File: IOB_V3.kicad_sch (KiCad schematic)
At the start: 6 parts, among them J1 Conn_01x02, J2 Conn_01x03, U1 REF3033

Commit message: WIP
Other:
- sheet MCU ports: added Vref_in; removed OCP_PWR_GOOD, SPI3_CLK, SPI3_MISO, SPI3_MOSI, SPI3_~{CS}

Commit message: WIP
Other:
- note added: "24V_PWR_Supply"

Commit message: WIP
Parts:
- added J18: Conn_01x08, Connector_IDC:IDC-Header_2x04_P2.54mm_Horizontal, symbol Connector_Generic:Conn_01x08
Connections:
- net GND: now also J18.8 (Pin_8)
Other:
- moved on the sheet: J2, U1

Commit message: WIP
for @Markus
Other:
- moved on the sheet: J1
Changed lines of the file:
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@@
     (comment 1 "Nathan Runggaldier")
   )
-  (junction (at 73.533 151.892) (diameter 0) (color 0 0 0 0)
+  (junction (at 71.247 151.892) (diameter 0) (color 0 0 0 0)
   )
   (junction (at 82.677 144.272) (diameter 0) (color 0 0 0 0)
@@
   )
   (junction (at 237.617 46.736) (diameter 0) (color 0 0 0 0)
-  )
-  (junction (at 71.501 144.272) (diameter 0) (color 0 0 0 0)
   )
   (junction (at 94.361 144.272) (diameter 0) (color 0 0 0 0)
@@
     (stroke (width 0) (type default) (color 0 0 0 0))
   )
-  (wire (pts (xy 71.501 144.272) (xy 71.501 144.399))
-    (stroke (width 0) (type default) (color 0 0 0 0))
-  )
   (wire (pts (xy 104.521 154.432) (xy 104.521 156.972))
     (stroke (width 0) (type default) (color 0 0 0 0))
@@
     (stroke (width 0) (type default) (color 0 0 0 0))
   )
-  (wire (pts (xy 73.533 151.892) (xy 73.533 153.289))
+  (wire (pts (xy 71.247 151.892) (xy 71.247 153.289))
     (stroke (width 0) (type default) (color 0 0 0 0))
   )
@@
     (stroke (width 0) (type default) (color 0 0 0 0))
   )
-  (wire (pts (xy 73.533 146.812) (xy 73.533 151.892))
+  (wire (pts (xy 71.247 146.812) (xy 71.247 151.892))
     (stroke (width 0) (type default) (color 0 0 0 0))
   )
@@
     (stroke (width 0) (type default) (color 0 0 0 0))
   )
+  (wire (pts (xy 69.215 144.272) (xy 82.677 144.272))
+    (stroke (width 0) (type default) (color 0 0 0 0))
+  )
   (wire (pts (xy 136.525 69.342) (xy 148.082 69.342))
     (stroke (width 0) (type default) (color 0 0 0 0))
   )
-  (wire (pts (xy 82.677 144.272) (xy 71.501 144.272))
-    (stroke (width 0) (type default) (color 0 0 0 0))
-  )
   (wire (pts (xy 198.12 97.663) (xy 188.595 97.663))
     (stroke (width 0) (type default) (color 0 0 0 0))
@@
     (stroke (width 0) (type default) (color 0 0 0 0))
   )
-  (wire (pts (xy 71.501 146.812) (xy 73.533 146.812))
+  (wire (pts (xy 69.215 146.812) (xy 71.247 146.812))
     (stroke (width 0) (type default) (color 0 0 0 0))
   )
@@
     (stroke (width 0) (type default) (color 0 0 0 0))
   )
-  (wire (pts (xy 73.533 151.892) (xy 66.421 151.892))
+  (wire (pts (xy 71.247 151.892) (xy 64.135 151.892))
     (stroke (width 0) (type default) (color 0 0 0 0))
   )
@@
     (effects (font (size 1.27 1.27)) (justify right bottom))
   )
-  (symbol (lib_id "power:GND") (at 73.533 153.289 0) (unit 1)
+  (symbol (lib_id "power:GND") (at 71.247 153.289 0) (unit 1)
     (in_bom yes) (on_board yes) (fields_autoplaced)
-    (property "Reference" "#PWR01" (id 0) (at 73.533 159.639 0)
-      (effects (font (size 1.27 1.27)) hide)
-    )
-    (property "Value" "GND" (id 1) (at 73.533 157.988 0))
-    (property "Footprint" "" (id 2) (at 73.533 153.289 0)
-      (effects (font (size 1.27 1.27)) hide)
-    )
-    (property "Datasheet" "" (id 3) (at 73.533 153.289 0)
+    (property "Reference" "#PWR01" (id 0) (at 71.247 159.639 0)
+      (effects (font (size 1.27 1.27)) hide)
+    )
+    (property "Value" "GND" (id 1) (at 71.247 157.988 0))
+    (property "Footprint" "" (id 2) (at 71.247 153.289 0)
+      (effects (font (size 1.27 1.27)) hide)
+    )
+    (property "Datasheet" "" (id 3) (at 71.247 153.289 0)
       (effects (font (size 1.27 1.27)) hide)
     )
@@
     (pin "3")
   )
-  (symbol (lib_id "Connector_Generic_MountingPin:Conn_01x02_MountingPin") (at 66.421 144.272 0) (mirror y) (unit 1)
+  (symbol (lib_id "Connector_Generic_MountingPin:Conn_01x02_MountingPin") (at 64.135 144.272 0) (mirror y) (unit 1)
     (in_bom yes) (on_board yes)
-    (property "Reference" "J1" (id 0) (at 66.421 141.732 0))
-    (property "Value" "Conn_01x02" (id 1) (at 68.5038 150.2156 0)
-      (effects (font (size 1.27 1.27)) hide)
-    )
-    (property "Footprint" "TXV_Library_Footprints:Molex_MicroFit_2Pin_Vertical" (id 2) (at 66.421 144.272 0)
-      (effects (font (size 1.27 1.27)) hide)
-    )
-    (property "Datasheet" "~" (id 3) (at 66.421 144.272 0)
+    (property "Reference" "J1" (id 0) (at 64.135 141.732 0))
+    (property "Value" "Conn_01x02" (id 1) (at 66.2178 150.2156 0)
+      (effects (font (size 1.27 1.27)) hide)
+    )
+    (property "Footprint" "TXV_Library_Footprints:Molex_MicroFit_2Pin_Vertical" (id 2) (at 64.135 144.272 0)
+      (effects (font (size 1.27 1.27)) hide)
+    )
+    (property "Datasheet" "~" (id 3) (at 64.135 144.272 0)
       (effects (font (size 1.27 1.27)) hide)
     )
@@
       (reference "#PWR0128") (unit 1) (value "GNDD") (footprint "")
     )
+    (path "/534d7b1f-d272-47da-b7a1-47aab2c48175/ecf47aa7-aedf-4e05-87ad-09faf807de95"
+      (reference "#PWR0129") (unit 1) (value "+5V") (footprint "")
+    )
     (path "/534d7b1f-d272-47da-b7a1-47aab2c48175/caec57d4-4051-45b0-9d96-83ec54018640"
       (reference "#PWR0130") (unit 1) (value "+3.3V") (footprint "")
     )
+    (path "/534d7b1f-d272-47da-b7a1-47aab2c48175/f0e15cc6-9ddb-41db-9a65-021037590f6d"
+      (reference "#PWR0131") (unit 1) (value "GNDD") (footprint "")
+    )
+    (path "/534d7b1f-d272-47da-b7a1-47aab2c48175/badff02a-39c9-4323-8c5b-17d78ddf24b3"
+      (reference "#PWR0132") (unit 1) (value "+3.3V") (footprint "")
+    )
     (path "/534d7b1f-d272-47da-b7a1-47aab2c48175/7dc5c5fa-cab7-41b7-b22c-69d8bb347819"
       (reference "#PWR0133") (unit 1) (value "+3.3V") (footprint "")
@@
       (reference "#PWR0138") (unit 1) (value "+5V") (footprint "")
     )
+    (path "/534d7b1f-d272-47da-b7a1-47aab2c48175/8eb43c8c-0075-4f4f-9aa4-067d574b0e90"
+      (reference "#PWR0139") (unit 1) (value "GNDD") (footprint "")
+    )
     (path "/534d7b1f-d272-47da-b7a1-47aab2c48175/573d7cc1-f5ea-48f8-9a0b-1e87d7df0d37"
       (reference "#PWR0140") (unit 1) (value "GNDD") (footprint "")
     )
+    (path "/534d7b1f-d272-47da-b7a1-47aab2c48175/7cb08f1b-dcb6-4ec8-a52d-cb4d654ba01c"
+      (reference "#PWR0141") (unit 1) (value "GNDA") (footprint "")
+    )
     (path "/534d7b1f-d272-47da-b7a1-47aab2c48175/60eaa4dd-d726-4d7e-a298-4ff4d8f59925"
       (reference "#PWR0142") (unit 1) (value "+5V") (footprint "")
@@
     )
     (path "/534d7b1f-d272-47da-b7a1-47aab2c48175/6878b1d1-3069-4d7c-b137-ec943b7a7195"
-      (reference "C9") (unit 1) (value "100n") (footprint "")
+      (reference "C9") (unit 1) (value "100n") (footprint "Capacitor_SMD:C_0603_1608Metric")
     )
     (path "/534d7b1f-d272-47da-b7a1-47aab2c48175/06ff87ca-8409-4f62-b5b9-dfff7179b28a"
@@
     )
     (path "/534d7b1f-d272-47da-b7a1-47aab2c48175/294f2165-b20b-4ebc-8f0e-881561e8f752"
-      (reference "C12") (unit 1) (value "100n") (footprint "")
+      (reference "C12") (unit 1) (value "100n") (footprint "Capacitor_SMD:C_0603_1608Metric")
     )
     (path "/534d7b1f-d272-47da-b7a1-47aab2c48175/6f9ecc9c-25f1-4f14-8b13-6d90691c29b8"
@@
     )
     (path "/534d7b1f-d272-47da-b7a1-47aab2c48175/a639352e-53e3-4cab-8b55-bde92bb637a1"
-      (reference "C16") (unit 1) (value "100n") (footprint "")
+      (reference "C16") (unit 1) (value "100n") (footprint "Capacitor_SMD:C_0603_1608Metric")
     )
     (path "/534d7b1f-d272-47da-b7a1-47aab2c48175/44748e99-2f16-4dbb-9b1f-4a0ec88f1a44"
-      (reference "C17") (unit 1) (value "100n") (footprint "")
+      (reference "C17") (unit 1) (value "100n") (footprint "Capacitor_SMD:C_0603_1608Metric")
     )
     (path "/534d7b1f-d272-47da-b7a1-47aab2c48175/d6093e36-a3f0-451c-9e60-7f87021e766f"
-      (reference "C18") (unit 1) (value "100n") (footprint "")
+      (reference "C18") (unit 1) (value "100n") (footprint "Capacitor_SMD:C_0603_1608Metric")
     )
     (path "/534d7b1f-d272-47da-b7a1-47aab2c48175/987eaacf-a0d3-47d1-878e-9f0be2f82cb7"
-      (reference "C19") (unit 1) (value "4.7u") (footprint "")
+      (reference "C19") (unit 1) (value "4.7u") (footprint "Capacitor_SMD:C_0603_1608Metric")
     )
     (path "/534d7b1f-d272-47da-b7a1-47aab2c48175/0f624398-c4ec-4016-aa2c-6a7e88a47a0d"
-      (reference "C20") (unit 1) (value "10n") (footprint "")
+      (reference "C20") (unit 1) (value "10n") (footprint "Capacitor_SMD:C_0603_1608Metric")
     )
     (path "/534d7b1f-d272-47da-b7a1-47aab2c48175/61e3f6a9-3d6c-43c5-9b6d-caf1b8e79e8d"
-      (reference "C21") (unit 1) (value "1u") (footprint "")
+      (reference "C21") (unit 1) (value "1u") (footprint "Capacitor_SMD:C_0603_1608Metric")
     )
     (path "/534d7b1f-d272-47da-b7a1-47aab2c48175/0524ab36-4a9f-428b-93d0-74e2071bb789"
-      (reference "C22") (unit 1) (value "100n") (footprint "")
+      (reference "C22") (unit 1) (value "100n") (footprint "Capacitor_SMD:C_0603_1608Metric")
     )
     (path "/534d7b1f-d272-47da-b7a1-47aab2c48175/03dd8607-6118-40cd-b14e-050b082cb085"
-      (reference "C23") (unit 1) (value "1u") (footprint "")
+      (reference "C23") (unit 1) (value "1u") (footprint "Capacitor_SMD:C_0603_1608Metric")
     )
     (path "/7ba2c87c-9f99-4884-a18b-49ccadb91960"
@@
       (reference "U15") (unit 1) (value "MCP1700-3302E_SOT23") (footprint "Package_TO_SOT_SMD:SOT-23")
     )
+    (path "/534d7b1f-d272-47da-b7a1-47aab2c48175/e2e54c0d-b3a2-4ce8-b51d-bacac6f7939d"
+      (reference "U16") (unit 1) (value "74LS151") (footprint "")
+    )
     (path "/534d7b1f-d272-47da-b7a1-47aab2c48175/53b56f53-5624-4871-a069-a1844c0f6f32"
       (reference "U17") (unit 1) (value "MCP2562FD") (footprint "Package_DFN_QFN:DFN-8-1EP_3x3mm_P0.65mm_EP1.55x2.4mm")
@@
       (reference "U18") (unit 1) (value "W25Q256JV") (footprint "TXV_Library_Footprints:WSON-8-8x6mm")
     )
-    (path "/534d7b1f-d272-47da-b7a1-47aab2c48175/c3b767f0-bf7e-4122-a31f-1b1385b0c8f2"
-      (reference "U19") (unit 1) (value "STM32G474MET6") (footprint "STM32:STM32G474MET3")
+    (path "/534d7b1f-d272-47da-b7a1-47aab2c48175/dd589c3e-1a73-40e3-b0dc-96c44ecf7431"
+      (reference "U19") (unit 1) (value "STM32G474MET3") (footprint "STM32:STM32G474MET3")
     )
     (path "/534d7b1f-d272-47da-b7a1-47aab2c48175/f4ff36c9-ec28-41a7-b279-9fca465de01b"

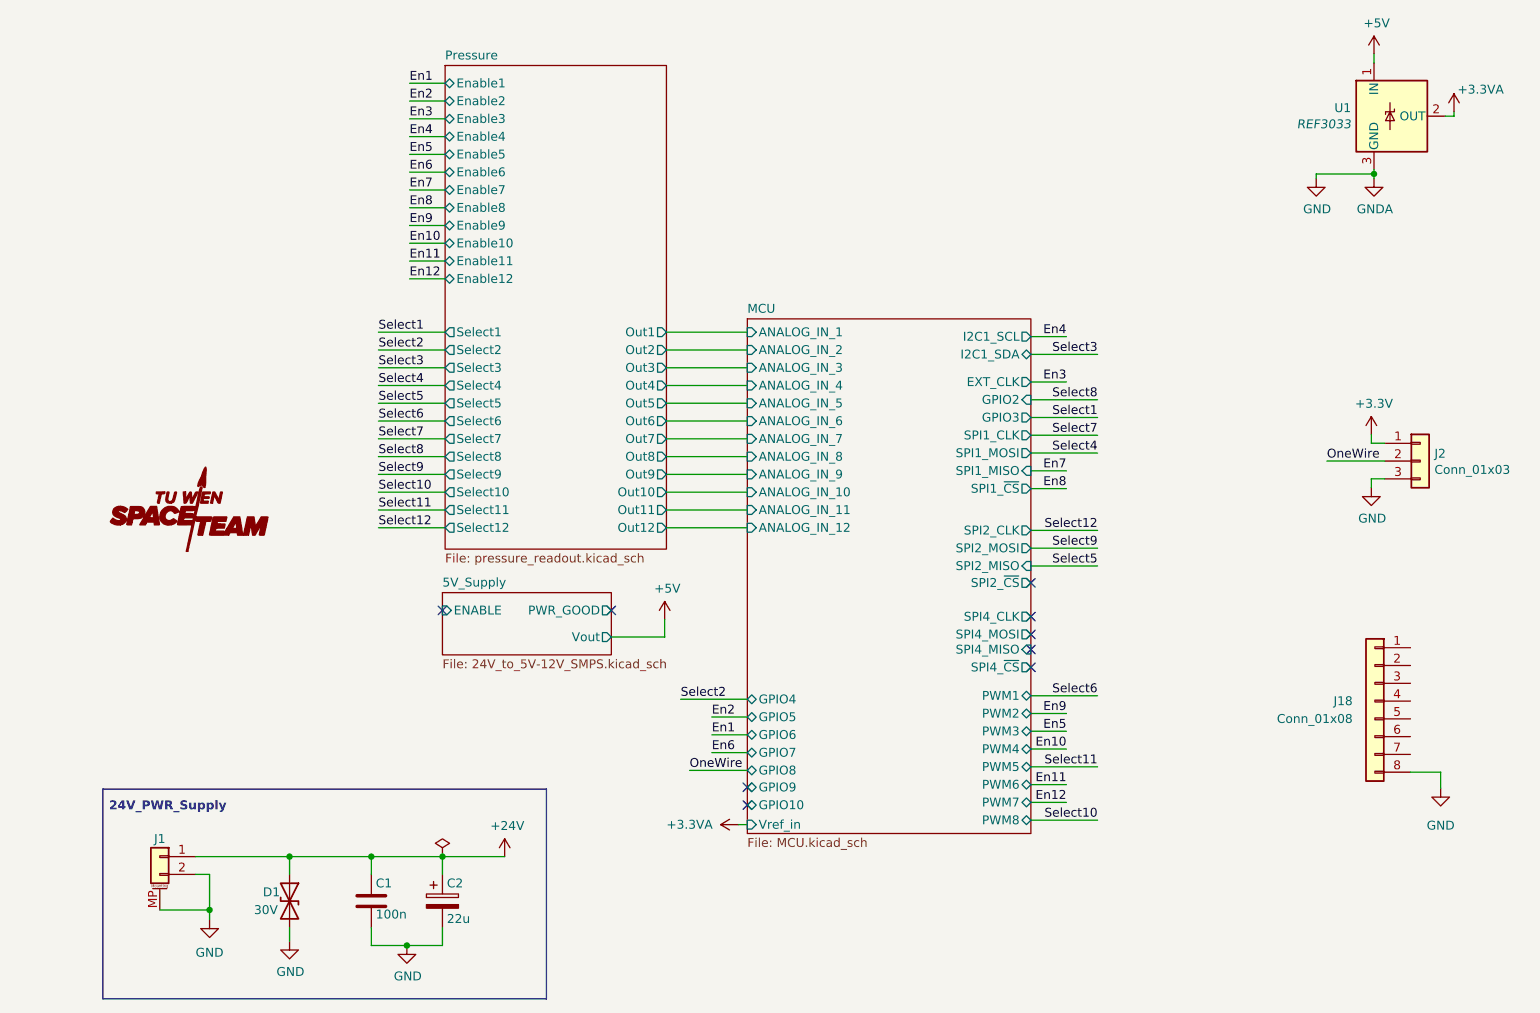
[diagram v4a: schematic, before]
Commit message: Schematic nearly complete
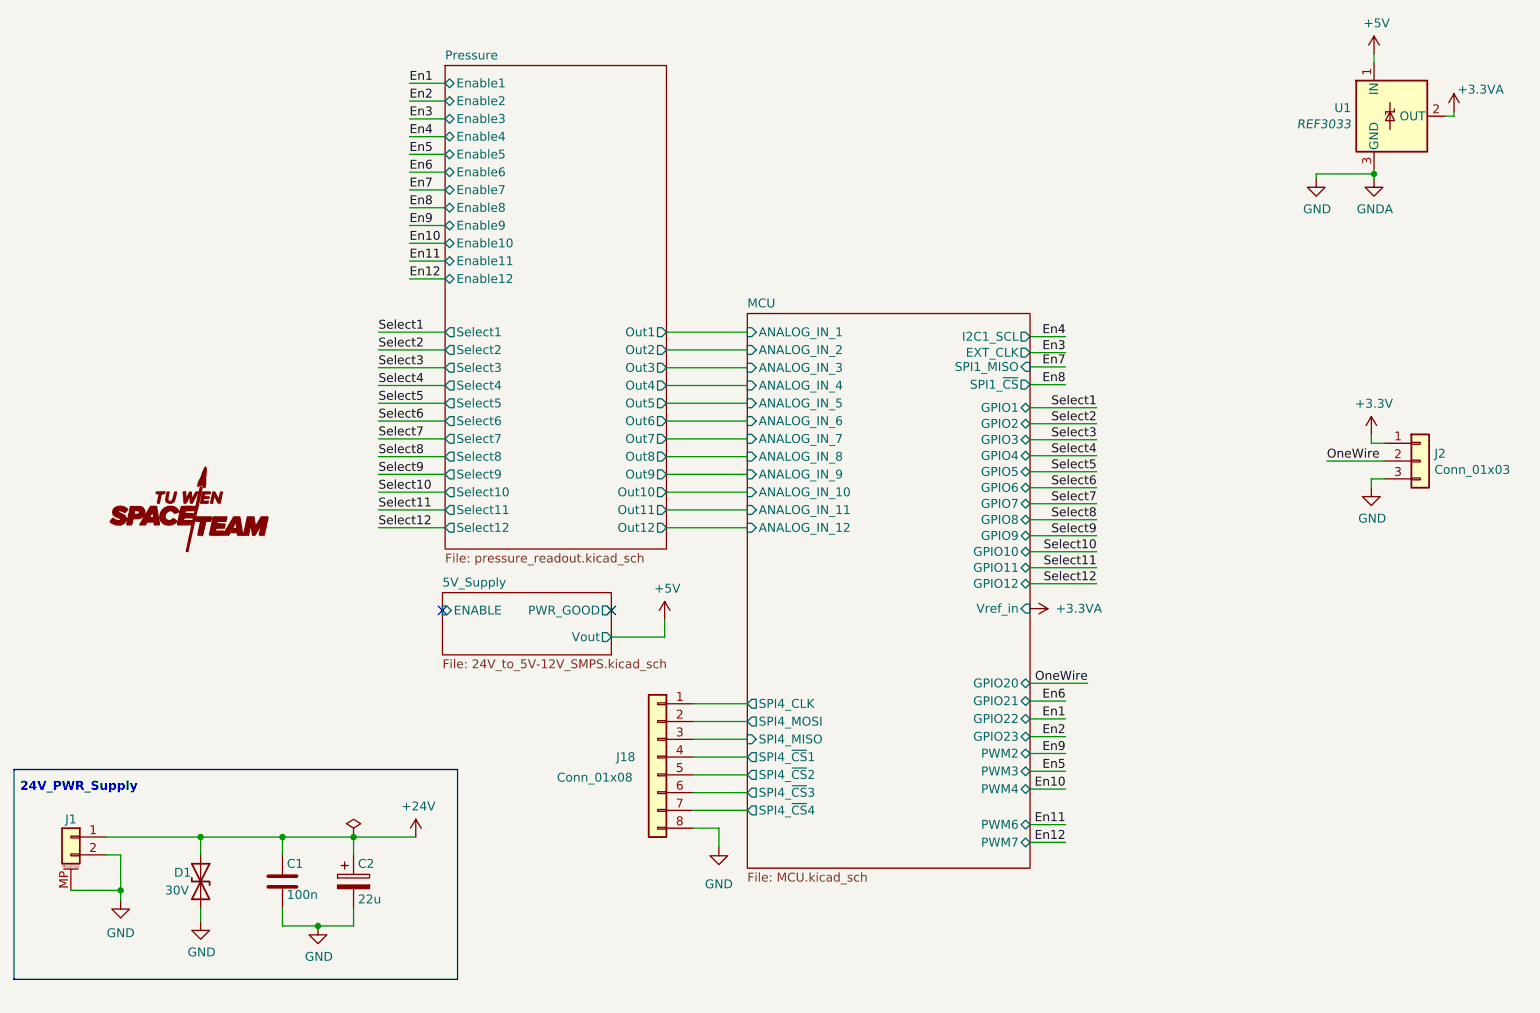
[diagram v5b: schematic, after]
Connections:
- net MCU/SPI4_CLK: now also J18.1 (Pin_1)
- net MCU/SPI4_MISO: now also J18.3 (Pin_3)
- net MCU/SPI4_MOSI: now also J18.2 (Pin_2)
- net MCU/SPI4_~{CS}1: now reaches J18.4 (Pin_4)
- net MCU/SPI4_~{CS}2: now reaches J18.5 (Pin_5)
- net MCU/SPI4_~{CS}3: now reaches J18.6 (Pin_6)
- net MCU/SPI4_~{CS}4: now reaches J18.7 (Pin_7)
- no-connect marks 9 -> 2
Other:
- sheet MCU ports: added GPIO1, GPIO11, GPIO12, GPIO20, GPIO21, GPIO22, GPIO23, SPI4_~{CS}1, SPI4_~{CS}2, SPI4_~{CS}3, SPI4_~{CS}4; removed I2C1_SDA, PWM1, PWM5, PWM8, SPI1_CLK, SPI1_MOSI, SPI2_CLK, SPI2_MISO, SPI2_MOSI, SPI2_~{CS}, SPI4_~{CS}
- moved on the sheet: C1, C2, D1, J1, J18

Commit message: Schematic ready for crosscheck
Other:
- moved on the sheet: J2, U1
